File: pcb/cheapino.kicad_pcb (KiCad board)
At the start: 2 copper layers, 152.2 x 95.1 mm, 65 parts, among them K1 SW_Push, K10 SW_Push, K11 SW_Push, K12 SW_Push, K13 SW_Push, K14 SW_Push, K15 SW_Push, K16 SW_Push, K17 SW_Push, K18 SW_Push, K19 K19, K2 SW_Push, K20 K20, K21 K21, K3 SW_Push, K4 SW_Push, K5 SW_Push, K6 SW_Push, K7 SW_Push, K8 SW_Push, K9 SW_Push, U1 RP2040-Zero

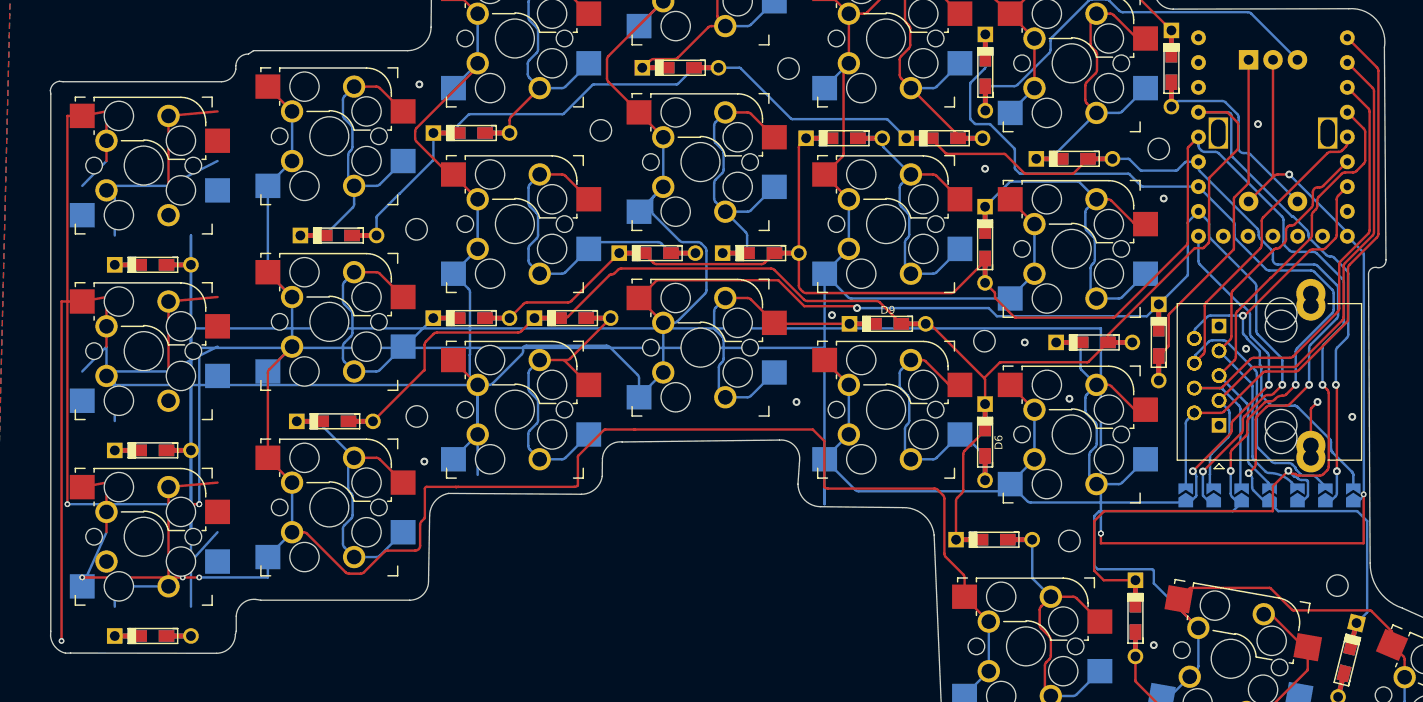
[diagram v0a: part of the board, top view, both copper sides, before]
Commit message: Finish 6-column matrix routing and NPTH-safe stitches
Reconnect ROW_4 / COL_1 / COL_2 with sequential on-board routes,
join the new column (K19/K20/K21 + D22/D23/D24) into the duplex
matrix, keep traces out of the bottom cutout and MX NPTH holes,
and add verify/patch scripts. Edge.Cuts remains a closed outline.

Zone fill and Gerbers still need a KiCad GUI pass before fab.
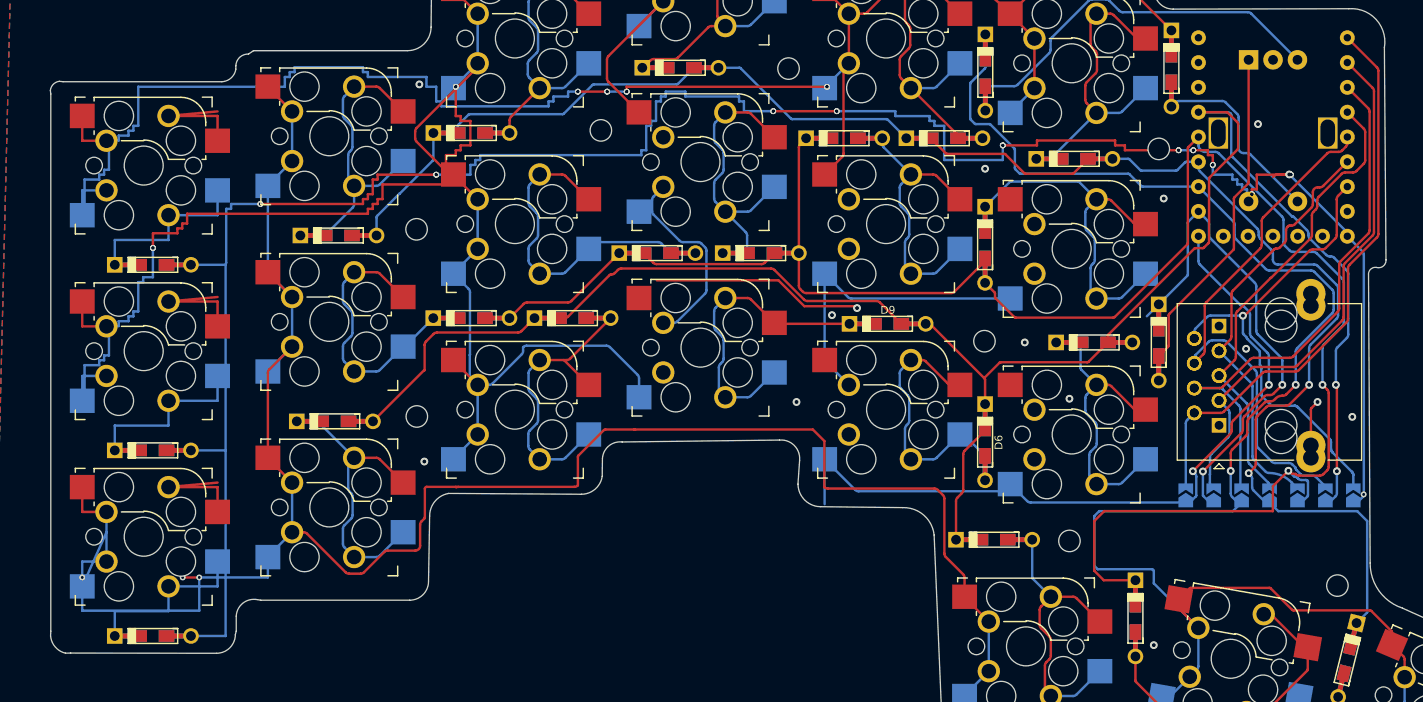
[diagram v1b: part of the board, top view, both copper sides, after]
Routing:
- net COL_1: track 411.9 -> 292.2 mm, vias 6 -> 10
- net COL_2: track 360.8 -> 287.8 mm, vias 4 -> 7
- net ROW_4: track 290.5 -> 230.6 mm, vias 5 -> 22
- net Net-(D22-K): track 12.2 -> 30.7 mm
- net COL_3: track 391.1 -> 406.6 mm
- net Net-(D23-K): track 28.4 -> 30.7 mm

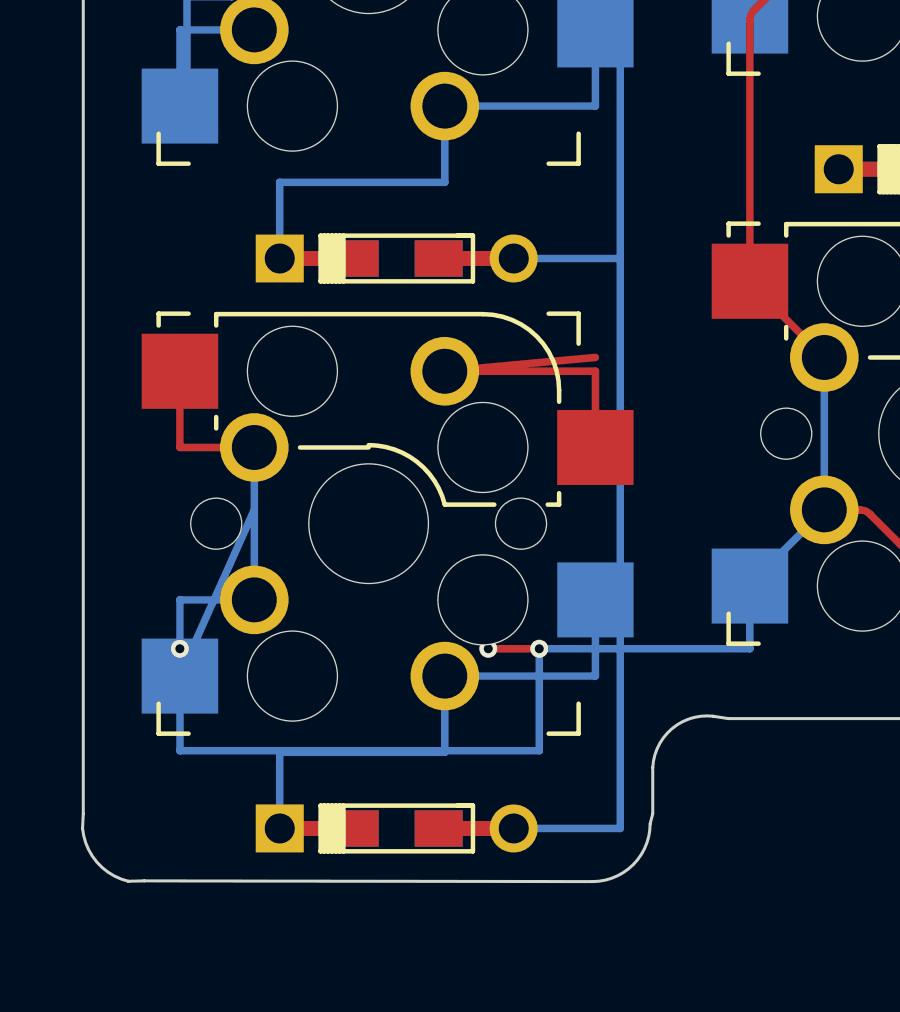
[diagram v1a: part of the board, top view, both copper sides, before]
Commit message: Fix K21 diode/column short and restore MX pad jumpers
Move Net-(D24-K) under K21 onto F.Cu so it no longer overlaps
the COL_3 B.Cu bypass. Mark duplicate MX/diode pads as jumpers
so KiCad 10 matches original Cheapino connectivity.
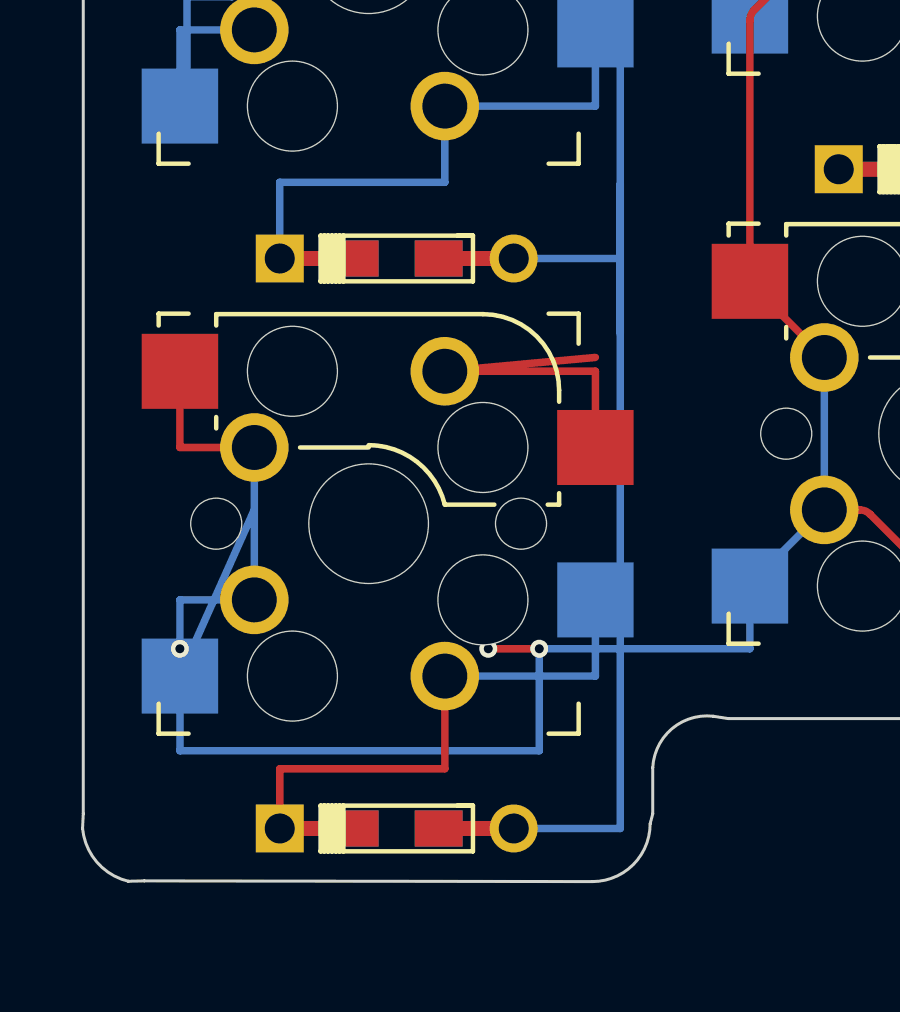
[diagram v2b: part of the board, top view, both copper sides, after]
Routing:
- net ROW_4: track 230.6 -> 235.6 mm

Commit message: Stitch remaining COL_2/K9, COL_3 via, and GND pours
Connect K9 pad 1 on F.Cu to the COL_2 run, join the K21 COL_3
via onto B.Cu, add GND vias on the new-column peninsula, and
solid-connect the GND zone so front/back pours stitch after fill.
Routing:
- net COL_2: track 287.8 -> 291.4 mm
- net COL_3: track 406.6 -> 408.3 mm
- net GND: vias 13 -> 19
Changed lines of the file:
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@@
+		(net "GND")
+	)
+	(segment
+		(start 102.5352 85.0784)
+		(end 100.72 85.0784)
+		(width 0.25)
+		(layer "F.Cu")
+		(net "COL_2")
+	)
+	(segment
+		(start 100.72 85.0784)
+		(end 100.72 86.893)
+		(width 0.25)
+		(layer "F.Cu")
+		(net "COL_2")
+	)
+	(segment
+		(start 54.0 115.5)
+		(end 55.7 115.5)
+		(width 0.25)
+		(layer "B.Cu")
+		(net "COL_3")
+	)
+	(via
+		(at 41.8 70.5)
+		(size 0.8)
+		(drill 0.4)
+		(layers "F.Cu" "B.Cu")
+		(free yes)
+		(capping no)
+		(covering
+			(front no)
+			(back no)
+		)
+		(plugging
+			(front no)
+			(back no)
+		)
+		(filling no)
+		(net "GND")
+	)
+	(via
+		(at 41.8 82.5)
+		(size 0.8)
+		(drill 0.4)
+		(layers "F.Cu" "B.Cu")
+		(free yes)
+		(capping no)
+		(covering
+			(front no)
+			(back no)
+		)
+		(plugging
+			(front no)
+			(back no)
+		)
+		(filling no)
+		(net "GND")
+	)
+	(via
+		(at 41.8 101.8)
+		(size 0.8)
+		(drill 0.4)
+		(layers "F.Cu" "B.Cu")
+		(free yes)
+		(capping no)
+		(covering
+			(front no)
+			(back no)
+		)
+		(plugging
+			(front no)
+			(back no)
+		)
+		(filling no)
+		(net "GND")
+	)
+	(via
+		(at 41.8 118.0)
+		(size 0.8)
+		(drill 0.4)
+		(layers "F.Cu" "B.Cu")
+		(free yes)
+		(capping no)
+		(covering
+			(front no)
+			(back no)
+		)
+		(plugging
+			(front no)
+			(back no)
+		)
+		(filling no)
+		(net "GND")
+	)
+	(via
+		(at 57.2 80.0)
+		(size 0.8)
+		(drill 0.4)
+		(layers "F.Cu" "B.Cu")
+		(free yes)
+		(capping no)
+		(covering
+			(front no)
+			(back no)
+		)
+		(plugging
+			(front no)
+			(back no)
+		)
+		(filling no)
+		(net "GND")
+	)
+	(via
+		(at 57.2 108.0)
+		(size 0.8)
+		(drill 0.4)
+		(layers "F.Cu" "B.Cu")
+		(free yes)
+		(capping no)
+		(covering
+			(front no)
+			(back no)
+		)
+		(plugging
+			(front no)
+			(back no)
+		)
+		(filling no)
 		(net "GND")
 	)
@@
 		(layers "F.Cu" "B.Cu")
 		(hatch edge 0.5)
-		(connect_pads
+		(connect_pads yes
 			(clearance 0.508)
 		)

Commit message: Close remaining COL_2/COL_3 via gaps and drop GND islands
Replace the COL_2 via that had no back-side copper with a via at
the F.Cu/B.Cu crossing by K9. Remove the unused COL_3 via under
K21. GND pour now deletes isolated islands after fill.
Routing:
- net COL_3: vias 5 -> 4
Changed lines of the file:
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@@
 		(net "COL_2")
 	)
-	(via
-		(at 123.0376 87.9227)
-		(size 0.8)
-		(drill 0.4)
-		(layers "F.Cu" "B.Cu")
-		(free yes)
-		(capping no)
-		(covering
-			(front no)
-			(back no)
-		)
-		(plugging
-			(front no)
-			(back no)
-		)
-		(filling no)
-		(net "COL_2")
-	)
-	(arc
+		(arc
 		(start 162.681047 99.015153)
 		(mid 162.57266 99.177365)
@@
 		(net "COL_3")
 	)
-	(via
-		(at 43.72 115.5)
-		(size 0.6)
-		(drill 0.3)
-		(layers "F.Cu" "B.Cu")
-		(capping no)
-		(covering
-			(front no)
-			(back no)
-		)
-		(plugging
-			(front no)
-			(back no)
-		)
-		(filling no)
-		(net "COL_3")
-	)
-	(via
+		(via
 		(at 167.9448 95.7834)
 		(size 0.8)
@@
 	)
 	(via
+		(at 107.62 85.078)
+		(size 0.8)
+		(drill 0.4)
+		(layers "F.Cu" "B.Cu")
+		(free yes)
+		(capping no)
+		(covering
+			(front no)
+			(back no)
+		)
+		(plugging
+			(front no)
+			(back no)
+		)
+		(filling no)
+		(net "COL_2")
+	)
+	(via
 		(at 140.208 91.44)
 		(size 0.8)
@@
 			(thermal_gap 0.5)
 			(thermal_bridge_width 0.5)
-			(island_removal_mode 0)
+			(island_removal_mode 1)
+			(island_area_min 10)
 		)
 		(polygon

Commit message: Connect encoder C/S2 to ROW_4 and tighten GND pour
Route ENC1 common and switch onto the ROW_4 backbone, remove the
one-sided ROW_4 via, and set GND zone pad clearance to 0 so vias
actually join the fill.
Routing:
- net ROW_4: track 235.6 -> 271.0 mm, vias 22 -> 21
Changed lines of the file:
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@@
 		(net "ROW_4")
 	)
-	(via
-		(at 174.9 107)
-		(size 0.6)
-		(drill 0.3)
-		(layers "F.Cu" "B.Cu")
-		(capping no)
-		(covering
-			(front no)
-			(back no)
-		)
-		(plugging
-			(front no)
-			(back no)
-		)
-		(filling no)
-		(net "ROW_4")
-	)
-	(arc
+		(arc
 		(start 165.741353 74.390647)
 		(mid 165.903565 74.28226)
@@
 		(net "COL_2")
 	)
+	(segment
+		(start 163.123 48.009)
+		(end 160.623 48.009)
+		(width 0.25)
+		(layer "B.Cu")
+		(net "ROW_4")
+	)
+	(segment
+		(start 160.623 48.009)
+		(end 160.623 62.509)
+		(width 0.25)
+		(layer "B.Cu")
+		(net "ROW_4")
+	)
+	(segment
+		(start 160.623 62.509)
+		(end 160.623 65.0)
+		(width 0.25)
+		(layer "B.Cu")
+		(net "ROW_4")
+	)
+	(segment
+		(start 160.623 65.0)
+		(end 165.5 65.0)
+		(width 0.25)
+		(layer "B.Cu")
+		(net "ROW_4")
+	)
+	(segment
+		(start 165.5 65.0)
+		(end 165.5 70.0)
+		(width 0.25)
+		(layer "B.Cu")
+		(net "ROW_4")
+	)
+	(segment
+		(start 165.5 70.0)
+		(end 167.284 70.0)
+		(width 0.25)
+		(layer "B.Cu")
+		(net "ROW_4")
+	)
+	(segment
+		(start 167.284 70.0)
+		(end 167.284 74.244)
+		(width 0.25)
+		(layer "B.Cu")
+		(net "ROW_4")
+	)
 	(via
 		(at 140.208 91.44)
@@
 		(hatch edge 0.5)
 		(connect_pads yes
-			(clearance 0.508)
+			(clearance 0)
 		)
 		(min_thickness 0.25)

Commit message: Stitch new-column GND pours through the board neck
Front and back GND fills on the extra column were isolated. Add a
0.5 mm dual-layer GND bridge at y=81.5 into the main board so both
pours join after zone fill.
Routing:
- net GND: track 7.26 -> 59.9 mm, vias 19 -> 20
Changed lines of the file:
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@@
 		(net "ROW_4")
+	)
+	(segment
+		(start 57.2 80.0)
+		(end 57.2 81.5)
+		(width 0.5)
+		(layer "F.Cu")
+		(net "GND")
+	)
+	(segment
+		(start 57.2 81.5)
+		(end 82.0 81.5)
+		(width 0.5)
+		(layer "F.Cu")
+		(net "GND")
+	)
+	(segment
+		(start 57.2 80.0)
+		(end 57.2 81.5)
+		(width 0.5)
+		(layer "B.Cu")
+		(net "GND")
+	)
+	(segment
+		(start 57.2 81.5)
+		(end 82.0 81.5)
+		(width 0.5)
+		(layer "B.Cu")
+		(net "GND")
+	)
+	(via
+		(at 82.0 81.5)
+		(size 0.8)
+		(drill 0.4)
+		(layers "F.Cu" "B.Cu")
+		(free yes)
+		(capping no)
+		(covering
+			(front no)
+			(back no)
+		)
+		(plugging
+			(front no)
+			(back no)
+		)
+		(filling no)
+		(net "GND")
 	)
 	(via

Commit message: Join COL_2 front/back islands and hit ENC1 pad C
Drop a via on the leftover COL_2 F.Cu stub and route B.Cu at y=89
to the MCU-side COL_2 track. Add ROW_4 copper on ENC1 pad C's
annular ring so KiCad sees the encoder common.
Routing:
- net COL_2: track 291.4 -> 322.8 mm, vias 7 -> 8
- net ROW_4: track 271.0 -> 274.6 mm
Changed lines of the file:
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@@
+	)
+	(via
+		(at 122.8465 87.7316)
+		(size 0.8)
+		(drill 0.4)
+		(layers "F.Cu" "B.Cu")
+		(free yes)
+		(capping no)
+		(covering
+			(front no)
+			(back no)
+		)
+		(plugging
+			(front no)
+			(back no)
+		)
+		(filling no)
+		(net "COL_2")
+	)
+	(segment
+		(start 122.8465 87.7316)
+		(end 122.8465 89.0)
+		(width 0.25)
+		(layer "B.Cu")
+		(net "COL_2")
+	)
+	(segment
+		(start 122.8465 89.0)
+		(end 152.7048 89.0)
+		(width 0.25)
+		(layer "B.Cu")
+		(net "COL_2")
+	)
+	(segment
+		(start 152.7048 89.0)
+		(end 152.7048 88.7592)
+		(width 0.25)
+		(layer "B.Cu")
+		(net "COL_2")
+	)
+	(segment
+		(start 159.7226 62.5094)
+		(end 161.5226 62.5094)
+		(width 0.25)
+		(layer "B.Cu")
+		(net "ROW_4")
+	)
+	(segment
+		(start 160.6226 61.6094)
+		(end 160.6226 63.4094)
+		(width 0.25)
+		(layer "B.Cu")
+		(net "ROW_4")
+	)
+	(segment
+		(start 167.284 74.244)
+		(end 167.2844 74.2442)
+		(width 0.25)
+		(layer "B.Cu")
+		(net "ROW_4")
 	)
 	(via

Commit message: Pour ROW_4 onto ENC1 pad C so KiCad 10 sees the connection
KiCad 10 does not treat a 0.25 mm track in the 1 mm hole as
connected. Add a small F/B pour and 0.8 mm bars on the annular
ring, clear of pads A/B.
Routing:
- net ROW_4: track 274.6 -> 285.3 mm
- added copper zone on B.Cu, net ROW_4
- added copper zone on F.Cu, net ROW_4
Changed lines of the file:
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@@
+		(net "ROW_4")
+	)
+	(zone
+		(net "ROW_4")
+		(net_name "ROW_4")
+		(layer "B.Cu")
+		(name "ENC1_C_ROW4")
+		(hatch edge 0.5)
+		(connect_pads
+			yes
+			(clearance 0)
+		)
+		(min_thickness 0.25)
+		(filled_areas_thickness no)
+		(fill
+			yes
+			(thermal_gap 0.2)
+			(thermal_bridge_width 0.5)
+		)
+		(polygon
+			(pts
+				(xy 159.5226 61.4094) (xy 161.7226 61.4094) (xy 161.7226 63.6094) (xy 159.5226 63.6094)
+			)
+		)
+	)
+	(zone
+		(net "ROW_4")
+		(net_name "ROW_4")
+		(layer "F.Cu")
+		(name "ENC1_C_ROW4")
+		(hatch edge 0.5)
+		(connect_pads
+			yes
+			(clearance 0)
+		)
+		(min_thickness 0.25)
+		(filled_areas_thickness no)
+		(fill
+			yes
+			(thermal_gap 0.2)
+			(thermal_bridge_width 0.5)
+		)
+		(polygon
+			(pts
+				(xy 159.5226 61.4094) (xy 161.7226 61.4094) (xy 161.7226 63.6094) (xy 159.5226 63.6094)
+			)
+		)
+	)
+	(segment
+		(start 160.6226 61.5594)
+		(end 160.6226 65.0)
+		(width 0.8)
+		(layer "B.Cu")
+		(net "ROW_4")
+	)
+	(segment
+		(start 159.67260000000002 62.5094)
+		(end 161.5726 62.5094)
+		(width 0.8)
+		(layer "B.Cu")
+		(net "ROW_4")
+	)
+	(segment
+		(start 160.6226 61.5594)
+		(end 160.6226 65.0)
+		(width 0.8)
+		(layer "F.Cu")
+		(net "ROW_4")
+	)
+	(segment
+		(start 159.67260000000002 62.5094)
+		(end 161.5726 62.5094)
+		(width 0.8)
+		(layer "F.Cu")
 		(net "ROW_4")
 	)
